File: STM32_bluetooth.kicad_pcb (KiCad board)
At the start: 4 copper layers, 0 parts

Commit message: started pcb layout.
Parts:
- added C1: 4u7, Capacitor_SMD:C_0402_1005Metric, F.Cu at (123.9, 84.1)
- added C10: 100n, Capacitor_SMD:C_0402_1005Metric, F.Cu at (126.8, 86.1)
- added C11: 100n, Capacitor_SMD:C_0402_1005Metric, F.Cu at (126.8, 88.1)
- added C12: 100n, Capacitor_SMD:C_0402_1005Metric, F.Cu at (126.8, 90.0)
- added C13: 10p, Capacitor_SMD:C_0402_1005Metric, F.Cu at (126.8, 92.0)
- added C14: 100n, Capacitor_SMD:C_0402_1005Metric, F.Cu at (126.8, 94.0)
- added C15: 10p, Capacitor_SMD:C_0402_1005Metric, F.Cu at (129.7, 84.1)
- added C16: 4u7, Capacitor_SMD:C_0603_1608Metric, F.Cu at (145.3, 89.4)
- added C17: 0.8p, Capacitor_SMD:C_0402_1005Metric, F.Cu at (129.7, 86.1)
- added C18: 0.3p, Capacitor_SMD:C_0402_1005Metric, F.Cu at (129.7, 88.1)
- added C19: 100n, Capacitor_SMD:C_0402_1005Metric, F.Cu at (129.7, 90.0)
- added C2: 4u7, Capacitor_SMD:C_0603_1608Metric, F.Cu at (145.3, 84.4)
- added C3: 100n, Capacitor_SMD:C_0402_1005Metric, F.Cu at (123.9, 86.1)
- added C4: 100n, Capacitor_SMD:C_0402_1005Metric, F.Cu at (123.9, 88.1)
- added C5: 4u7, Capacitor_SMD:C_0402_1005Metric, F.Cu at (123.9, 90.0)
- added C6: 100n, Capacitor_SMD:C_0402_1005Metric, F.Cu at (123.9, 92.0)
- added C7: 100n, Capacitor_SMD:C_0402_1005Metric, F.Cu at (123.9, 94.0)
- added C8: 100n, Capacitor_SMD:C_0402_1005Metric, F.Cu at (126.8, 84.1)
- added C9: 4u7, Capacitor_SMD:C_0603_1608Metric, F.Cu at (145.3, 86.9)
- added D1: LED, LED_SMD:LED_0402_1005Metric, F.Cu at (149.0, 99.5)
- added FLT1: DLF162500LT-5028A1, STM32_bluetooth_PCB_footprint:DLF162500LT-5028A1, F.Cu at (148.9, 90.7)
- added J1: USB_C_Receptacle_USB2.0_16P, Connector_USB:USB_C_Receptacle_GCT_USB4105-xx-A_16P_TopMnt_Horizontal, F.Cu at (128.3, 78.4)
- added J2: Conn_01x04_Pin, Connector_Molex:Molex_PicoBlade_53048-0410_1x04_P1.25mm_Horizontal, F.Cu at (136.5, 94.5)
- added J3: Conn_ARM_SWD_TagConnect_TC2030, Connector:Tag-Connect_TC2030-IDC-FP_2x03_P1.27mm_Vertical, F.Cu at (139.0, 77.9)
- added J4: Conn_Coaxial, Connector_Coaxial:U.FL_Hirose_U.FL-R-SMT-1_Vertical, F.Cu at (145.3, 95.5)
- added L1: 10u, Inductor_SMD:L_0402_1005Metric, F.Cu at (149.6, 93.5)
- added L2: L, Inductor_SMD:L_0805_2012Metric, F.Cu at (145.1, 99.9)
- added L3: 2.7n, Inductor_SMD:L_0402_1005Metric, F.Cu at (149.6, 95.4)
- added R1: 5.1k, Capacitor_SMD:C_0402_1005Metric, F.Cu at (129.7, 92.0)
- added R2: 5.1k, Capacitor_SMD:C_0402_1005Metric, F.Cu at (129.7, 94.0)
- added R3: 220R, Capacitor_SMD:C_0402_1005Metric, F.Cu at (132.5, 84.1)
- added R4: 220R, Capacitor_SMD:C_0402_1005Metric, F.Cu at (132.5, 86.1)
- added R5: 220R, Capacitor_SMD:C_0402_1005Metric, F.Cu at (132.5, 88.1)
- added R6: 5.1k, Capacitor_SMD:C_0402_1005Metric, F.Cu at (132.5, 90.0)
- added R7: 220R, Capacitor_SMD:C_0402_1005Metric, F.Cu at (132.5, 92.0)
- added SW1: SW_Push, Button_Switch_SMD:SW_SPST_CK_RS282G05A3, F.Cu at (127.9, 97.5)
- added U1: MIC5365-3.3YD5, Package_TO_SOT_SMD:SOT-23-5, F.Cu at (145.8, 75.6)
- added U2: USBLC6-2SC6, Package_TO_SOT_SMD:SOT-23-6, F.Cu at (145.8, 80.2)
- added U3: STM32WB55CEU6, Package_DFN_QFN:QFN-48-1EP_7x7mm_P0.5mm_EP5.6x5.6mm, F.Cu at (90.7, 90.7)
- added X1: 32kHz768, Crystal:Crystal_SMD_2012-2Pin_2.0x1.2mm, F.Cu at (149.1, 88.2)
- added X2: 32MHz, Crystal:Crystal_SMD_2016-4Pin_2.0x1.6mm, F.Cu at (149.2, 85.0)

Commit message: board layout completed
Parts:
- moved U1 89.0 mm to (61.8, 104.9), turned to -90 degrees
- moved U2 86.1 mm to (61.8, 99.1)
- moved J2 82.9 mm to (54.7, 108.1), turned to -90 degrees
- moved J1 76.9 mm to (53.8, 97.6), turned to -90 degrees
- moved R1 75.7 mm to (54.8, 103.6)
- moved R2 74.9 mm to (54.8, 91.6)
- moved C2 72.3 mm to (76.2, 106.0), turned to -90 degrees
- moved J3 72.0 mm to (70.8, 101.2), turned to -90 degrees
- moved X1 71.7 mm to (79.7, 106.2), turned to 180 degrees
- moved L1 69.6 mm to (80.0, 95.0), turned to 90 degrees
- moved C9 68.0 mm to (77.6, 93.0), turned to 180 degrees
- moved L2 64.4 mm to (81.0, 93.0)
- moved C1 64.2 mm to (62.3, 102.1), turned to 180 degrees
- moved X2 64.1 mm to (85.8, 94.0), turned to 90 degrees
- moved C5 64.0 mm to (62.4, 107.6), turned to 180 degrees
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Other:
- board outline added: 50.8 x 26 mm

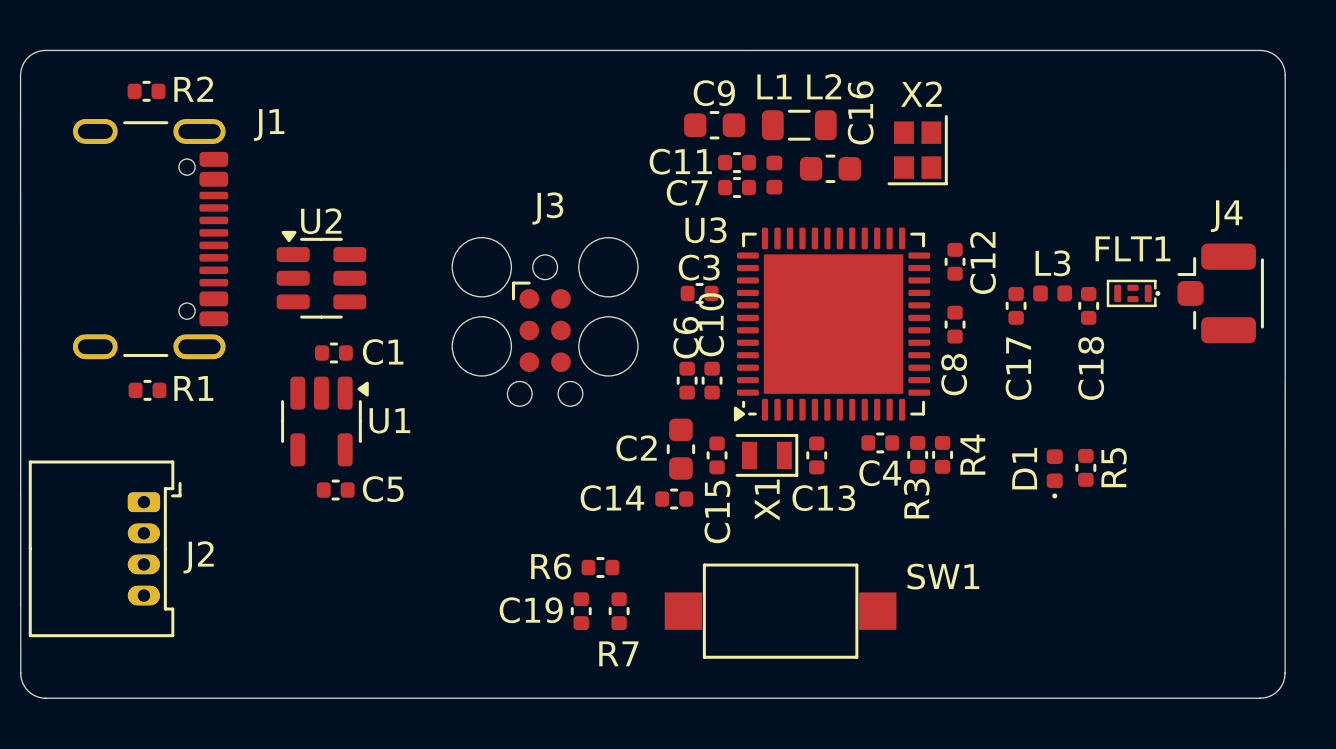
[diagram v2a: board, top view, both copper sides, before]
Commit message: Added via's and tracing for RF circuit.
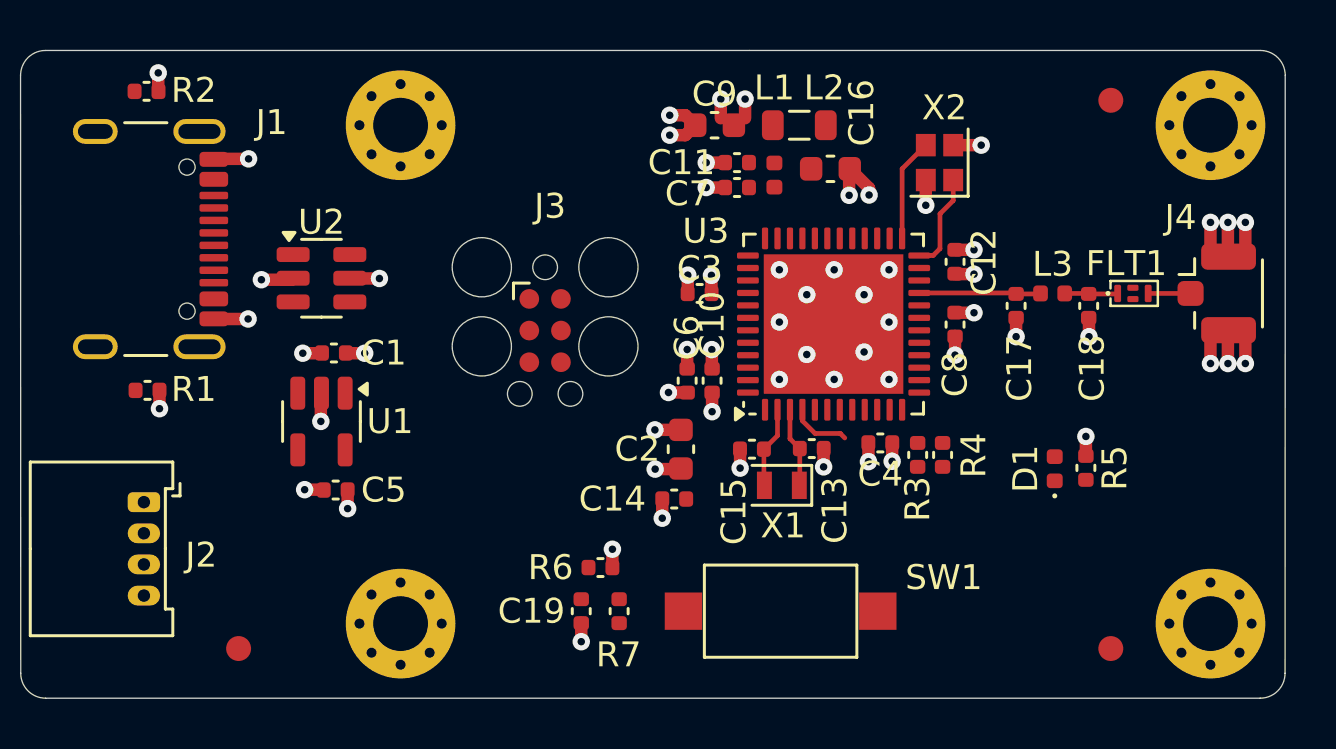
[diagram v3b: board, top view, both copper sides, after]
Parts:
- added FM1: Fiducial, Fiducial:Fiducial_1mm_Mask2mm, F.Cu at (93.5, 114.0)
- added FM2: Fiducial, Fiducial:Fiducial_1mm_Mask2mm, F.Cu at (58.5, 114.0)
- added FM3: Fiducial, Fiducial:Fiducial_1mm_Mask2mm, F.Cu at (93.5, 92.0)
- added H1: MountingHole_Pad, MountingHole:MountingHole_2.2mm_M2_Pad_Via, F.Cu at (97.5, 113.0)
- added H2: MountingHole_Pad, MountingHole:MountingHole_2.2mm_M2_Pad_Via, F.Cu at (97.5, 93.0)
- added H3: MountingHole_Pad, MountingHole:MountingHole_2.2mm_M2_Pad_Via, F.Cu at (65.0, 93.0)
- added H4: MountingHole_Pad, MountingHole:MountingHole_2.2mm_M2_Pad_Via, F.Cu at (65.0, 113.0)
- moved C15 1.42 mm to (79.1, 106.0), turned to 180 degrees
- moved X1 1.34 mm to (80.3, 107.5)
- moved X2 1.01 mm to (86.6, 94.5)
- moved C13 0.34 mm to (81.5, 106.0), turned to 0 degrees
- turned FLT1 to 0 degrees
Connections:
- C12 pad 1: +3V3 -> +3.3V
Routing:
- net GND: track 0.00 -> 35.3 mm, vias 0 -> 49
- net +3V3: track 0.00 -> 6.16 mm
- net /RF: track 0.00 -> 4.89 mm
- net /HSE_IN: track 0.00 -> 4.14 mm
- net /HSE_OUT: track 0.00 -> 3.92 mm
- net /LSE_IN: track 0.00 -> 3.27 mm
- net /LSE_OUT: track 0.00 -> 3.20 mm
- net /BOOT0: track 0.00 -> 2.43 mm
- net /RF_MATCH: track 0.00 -> 2.14 mm
- net /RF_ANT: track 0.00 -> 1.70 mm
- net +5V: track 0.00 -> 1.54 mm, vias 0 -> 2
- net +3.3V: track 0.00 -> 1.52 mm, vias 0 -> 10
- added copper zone on In1.Cu, net GND
- added copper zone on In2.Cu, net GND

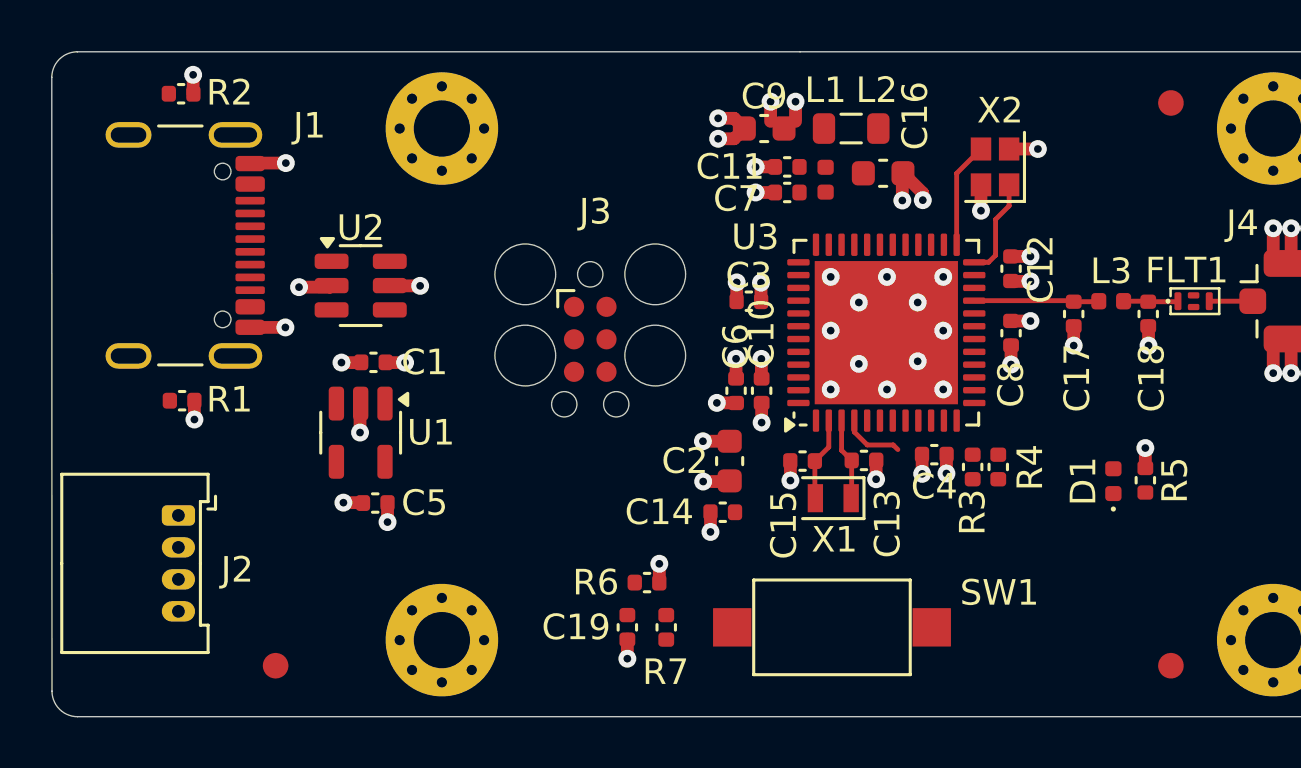
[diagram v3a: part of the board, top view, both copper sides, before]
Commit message: finished via's, finished tracing, still need to connect ground pins.
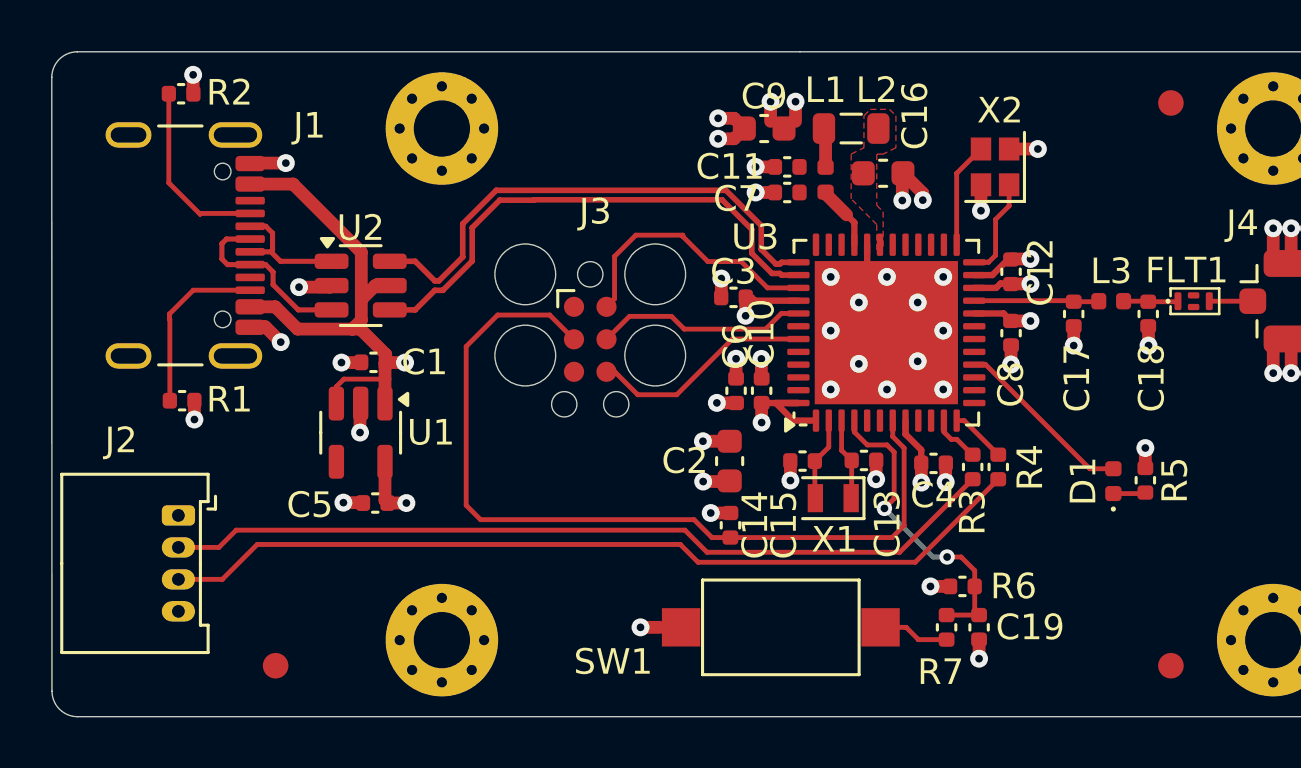
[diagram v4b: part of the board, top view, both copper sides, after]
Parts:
- moved C19 13.8 mm to (86.0, 112.5)
- moved R6 12.3 mm to (85.3, 110.9), turned to 180 degrees
- moved R7 11.0 mm to (84.7, 112.5)
- moved SW1 2.00 mm to (78.2, 112.5), turned to 180 degrees
- moved C3 0.62 mm to (76.4, 99.6)
- moved C14 0.59 mm to (76.3, 108.5), turned to -90 degrees
- moved C4 0.34 mm to (84.2, 106.1)
- moved C12 0.12 mm to (87.2, 98.6)
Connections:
- U3 pad 23: +3V3 -> +3.3V
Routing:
- net /UART_RXC: track 0.00 -> 34.2 mm
- net /SWD_NRST: track 0.00 -> 33.5 mm
- net /UART_TXC: track 0.00 -> 32.9 mm
- net /USB_D+: track 0.00 -> 20.3 mm
- net /USB_D-: track 0.00 -> 20.3 mm
- net +5V: track 1.54 -> 21.4 mm, vias 2 -> 1
- net +3V3: track 6.16 -> 16.7 mm
- net /SWD_DIO: track 0.00 -> 10.5 mm
- net /BOOT0: track 2.43 -> 12.3 mm, vias 0 -> 2
- net /SWD_TRC: track 0.00 -> 8.78 mm
- net /SWD_CLK: track 0.00 -> 8.33 mm
- net /USB_CC1: track 0.00 -> 7.18 mm
- net Net-(J1-D+-PadA6): track 0.00 -> 7.18 mm
- net /LED_A: track 0.00 -> 7.12 mm
- net /USB_CC2: track 0.00 -> 6.94 mm
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- added copper zone on In1.Cu, net +3.3V
- added copper zone on In2.Cu, net +3.3V
- added copper zone on F.Cu, net /SMPSFB

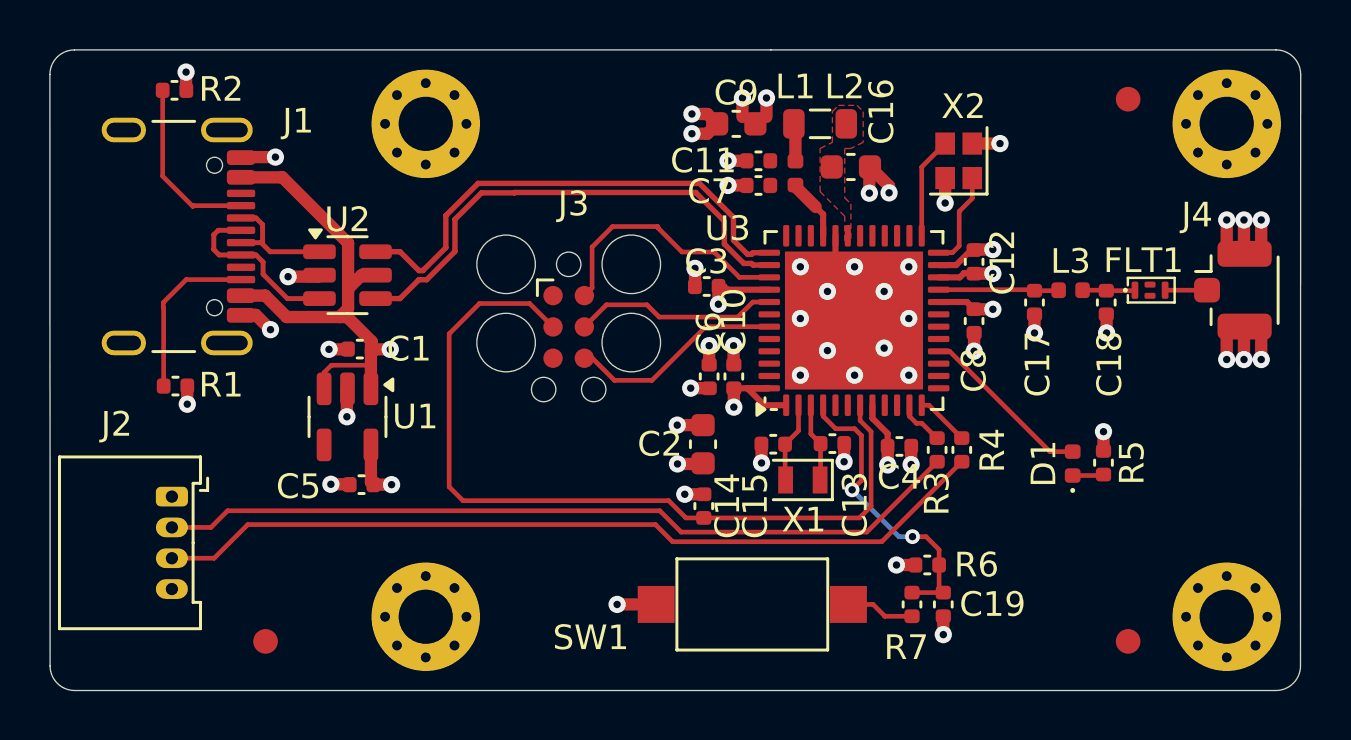
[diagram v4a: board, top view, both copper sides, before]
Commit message: finished the layout, the connections, silkscreen.
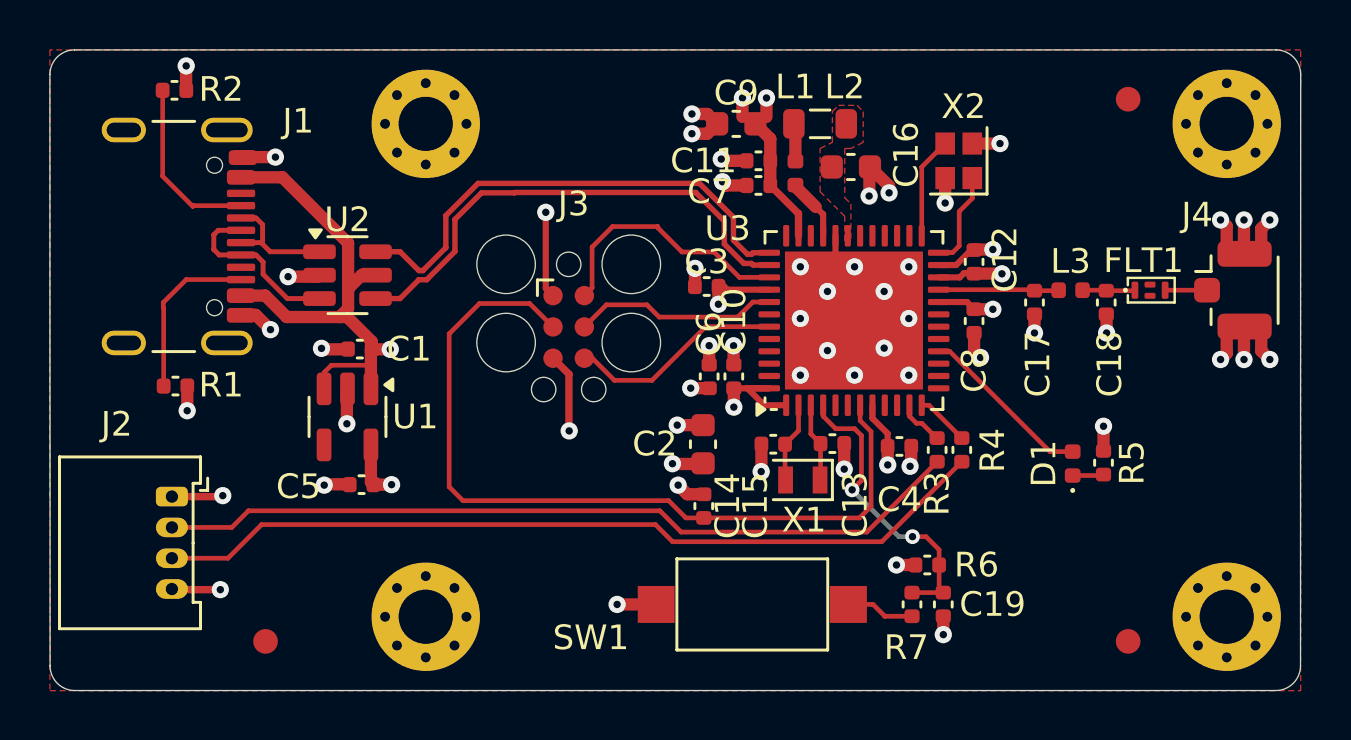
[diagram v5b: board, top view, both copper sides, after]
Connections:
- J3 pad 1: +3V3 -> +3.3V
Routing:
- net GND: track 40.7 -> 50.6 mm, vias 49 -> 51
- net +3.3V: track 4.86 -> 10.4 mm, vias 11 -> 13
- net +3V3: track 16.7 -> 22.0 mm
- added copper zone on F.Cu, net GND
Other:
- rule pad_to_mask_clearance: 0.08 -> 0
